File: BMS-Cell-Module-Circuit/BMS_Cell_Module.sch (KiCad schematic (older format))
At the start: 34 parts, among them J1 Conn_01x02_Female, J2 Conn_01x04_Female, J3 Conn_01x04_Female, J4 Conn Female, J5 Conn Male, M1 SI2312BDS-T1-E3, U1 MCP1703A-3302_SOT223, U2 ADUM1250ARZ, U3 ATTINY85-20SU

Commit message: Project file changes
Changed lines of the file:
@@
 Text GLabel 10400 5400 2    60   Input ~ 12
 GND2
-Text Notes 5750 4450 2    60   ~ 0
+Text Notes 5750 4250 2    60   ~ 0
 Input battery voltage resistor \ndivider 517K vs 680K\n4.5V maps to 2.55V
 Text Notes 1150 5350 0    60   ~ 0
@@
 P 1250 5550
 F 0 "D1" H 1250 5650 50  0000 C CNN
-F 1 "SE30AFG-M3/6A" V 1150 5900 50  0000 C CNN
+F 1 "SE30AFG-M3/6A" V 1250 6050 50  0000 C CNN
 F 2 "Diodes_SMD:D_SMA" H 1250 5550 50  0001 C CNN
 F 3 "http://uk.farnell.com/vishay/se30afg-m3-6a/rectifier-esd-400v-3a-do-221ac/dp/2313878" H 1250 5550 50  0001 C CNN
@@
 P 1650 5550
 F 0 "F1" V 1730 5550 50  0000 C CNN
-F 1 "MC36232 1.5A 24V" V 1850 6150 50  0000 C CNN
+F 1 "MC36232 1.5A 24V" V 1550 5650 50  0000 C CNN
 F 2 "Resistors_SMD:R_1812_HandSoldering" V 1580 5550 50  0001 C CNN
 F 3 "http://uk.farnell.com/multicomp/mc36232/fuse-ptc-reset-smd-24v-1-5a/dp/1861171" H 1650 5550 50  0001 C CNN
@@
 U 1 1 5A08E265
 P 5600 6650
-F 0 "J5" H 5600 6950 50  0000 C CNN
-F 1 "Conn Male" H 5700 6200 50  0000 C CNN
+F 0 "J5" H 5600 7150 50  0000 C CNN
+F 1 "Conn Male" V 5550 6650 50  0000 C CNN
 F 2 "Pin_Headers:Pin_Header_Angled_1x10_Pitch2.54mm" H 5600 6650 50  0001 C CNN
 F 3 "" H 5600 6650 50  0001 C CNN
@@
 U 1 1 5A08F09E
 P 5250 6650
-F 0 "J4" H 5250 6950 50  0000 C CNN
-F 1 "Conn Female" H 5200 7050 50  0000 C CNN
+F 0 "J4" H 5300 7150 50  0000 C CNN
+F 1 "Conn Female" V 5300 6650 50  0000 C CNN
 F 2 "Socket_Strips:Socket_Strip_Angled_1x10_Pitch2.54mm" H 5250 6650 50  0001 C CNN
 F 3 "" H 5250 6650 50  0001 C CNN
@@
 	1    0    0    -1
 $EndComp
-Text GLabel 5800 7400 2    60   Input ~ 0
+Text GLabel 5900 7150 2    60   Input ~ 0
 GND2
 Text GLabel 1400 5050 1    60   Input ~ 12
@@
 Connection ~ 3800 3400
 Wire Wire Line
-	6200 2550 6200 6750
-Wire Wire Line
-	6050 2550 6050 6950
+	6200 2550 6200 3100
+Wire Wire Line
+	6200 3100 6200 6750
+Wire Wire Line
+	6050 2550 6050 3500
+Wire Wire Line
+	6050 3500 6050 6950
 Connection ~ 6350 3500
 Connection ~ 6050 3500
@@
 Connection ~ 6200 3100
 Wire Wire Line
-	6350 2550 6350 3500
+	6350 2550 6350 3250
+Wire Wire Line
+	6350 3250 6350 3400
+Wire Wire Line
+	6350 3400 6350 3500
 Wire Wire Line
 	6350 3400 6350 3250
@@
 Connection ~ 9600 5400
 Wire Wire Line
-	9350 4900 9800 4900
+	9350 4900 9400 4900
+Wire Wire Line
+	9400 4900 9600 4900
+Wire Wire Line
+	9600 4900 9800 4900
 Connection ~ 9600 4900
 Wire Wire Line
@@
 Connection ~ 9700 5400
 Wire Wire Line
-	5450 5050 5450 5450
+	5450 5050 5450 5200
+Wire Wire Line
+	5450 5200 5450 5450
 Wire Wire Line
 	5450 5750 5450 5850
@@
 	4200 5150 4600 5150
 Wire Wire Line
-	4200 5150 4200 5450
+	4200 5150 4200 5400
+Wire Wire Line
+	4200 5400 4200 5450
 Wire Wire Line
 	4200 3400 4200 4850
@@
 Connection ~ 5450 5850
 Wire Wire Line
-	4200 5400 6650 5400
+	4200 5400 6450 5400
+Wire Wire Line
+	6450 5400 6650 5400
 Connection ~ 4200 5400
 Wire Wire Line
-	10300 4150 10300 4400
+	10300 4150 10300 4250
+Wire Wire Line
+	10300 4250 10300 4400
 Wire Wire Line
 	10300 3850 10300 3750
@@
 	10300 4700 10300 4750
 Wire Wire Line
-	9350 5400 10400 5400
+	9350 5400 9600 5400
+Wire Wire Line
+	9600 5400 9700 5400
+Wire Wire Line
+	9700 5400 10300 5400
+Wire Wire Line
+	10300 5400 10400 5400
 Connection ~ 10300 5400
 Wire Wire Line
@@
 	6150 4250 6150 5000
 Wire Wire Line
-	6100 5000 6650 5000
+	6100 5000 6150 5000
+Wire Wire Line
+	6150 5000 6650 5000
 Connection ~ 10300 4250
 Wire Wire Line
@@
 	5950 1300 5900 1400
 Wire Wire Line
-	5900 1400 5900 1850
-Wire Wire Line
-	6050 1300 6050 1850
-Wire Wire Line
-	6200 1400 6200 1850
+	5900 1400 5900 1550
+Wire Wire Line
+	5900 1550 5900 1850
+Wire Wire Line
+	6050 1300 6050 1600
+Wire Wire Line
+	6050 1600 6050 1850
+Wire Wire Line
+	6200 1400 6200 1650
+Wire Wire Line
+	6200 1650 6200 1850
 Wire Wire Line
 	6200 1400 6150 1300
@@
 	6250 1300 6350 1400
 Wire Wire Line
-	6350 1400 6350 1850
+	6350 1400 6350 1700
+Wire Wire Line
+	6350 1700 6350 1850
 Wire Wire Line
 	6350 1700 7050 1700
@@
 Connection ~ 5850 5850
 Wire Wire Line
-	1700 6100 1700 7250
-Wire Wire Line
-	1550 6850 2150 6850
-Wire Wire Line
-	3050 6850 3050 7250
+	1700 6100 1700 6850
+Wire Wire Line
+	1700 6850 1700 7250
+Wire Wire Line
+	1550 6850 1700 6850
+Wire Wire Line
+	1700 6850 2150 6850
+Wire Wire Line
+	3050 6850 3050 7100
+Wire Wire Line
+	3050 7100 3050 7250
 Connection ~ 1700 6850
 Wire Wire Line
@@
 	800  5550 800  5800
 Wire Wire Line
-	800  5550 1100 5550
+	800  5550 1050 5550
+Wire Wire Line
+	1050 5550 1100 5550
 Wire Wire Line
 	1400 5550 1500 5550
@@
 	3450 6950 4550 6950
 Wire Wire Line
-	4550 6550 4550 7000
-Wire Wire Line
-	3700 7450 5050 7450
-Wire Wire Line
-	5050 7150 5050 7550
+	4550 6550 4550 6950
+Wire Wire Line
+	4550 6950 4550 7000
+Wire Wire Line
+	3700 7450 4550 7450
+Wire Wire Line
+	4550 7450 5050 7450
+Wire Wire Line
+	5050 7150 5050 7450
+Wire Wire Line
+	5050 7450 5150 7450
 Wire Wire Line
 	6650 5300 6150 5300
@@
 	6150 6550 5800 6550
 Wire Wire Line
-	4200 5850 9700 5850
+	4200 5850 5450 5850
+Wire Wire Line
+	5450 5850 5700 5850
+Wire Wire Line
+	5700 5850 5850 5850
+Wire Wire Line
+	5850 5850 9700 5850
 Connection ~ 1950 5550
 Wire Wire Line
-	2750 3400 3050 3400
+	2750 3400 2900 3400
+Wire Wire Line
+	2900 3400 3050 3400
 Wire Wire Line
 	4050 3400 4050 3550
 Connection ~ 4050 3400
 Wire Wire Line
-	3650 3400 6450 3400
-Wire Wire Line
-	2600 3050 5900 3050
-Wire Wire Line
-	5150 5200 6650 5200
+	3650 3400 3800 3400
+Wire Wire Line
+	3800 3400 3900 3400
+Wire Wire Line
+	3900 3400 4050 3400
+Wire Wire Line
+	4050 3400 4200 3400
+Wire Wire Line
+	4200 3400 6350 3400
+Wire Wire Line
+	6350 3400 6450 3400
+Wire Wire Line
+	2600 3050 2900 3050
+Wire Wire Line
+	2900 3050 3350 3050
+Wire Wire Line
+	3350 3050 3800 3050
+Wire Wire Line
+	3800 3050 5600 3050
+Wire Wire Line
+	5600 3050 5900 3050
+Wire Wire Line
+	5150 5200 5450 5200
+Wire Wire Line
+	5450 5200 5700 5200
+Wire Wire Line
+	5700 5200 6650 5200
 Wire Wire Line
 	1150 5050 1150 4800
@@
 Wire Wire Line
 	1950 6100 1950 5550
-Text GLabel 5050 7550 2    60   Input ~ 0
+Text GLabel 5150 7450 2    60   Input ~ 0
 GND
 Connection ~ 5050 7450
@@
 Wire Wire Line
 	5050 6850 5050 6950
-Connection ~ 3050 6850
 Wire Wire Line
 	5450 4300 5950 4300
@@
 	2750 5950 5800 5950
 Wire Wire Line
-	5800 7150 5800 7400
+	5800 7150 5900 7150
 Wire Wire Line
 	5800 7050 6450 7050
@@
 	900  5150 1050 5250
 Wire Wire Line
-	1050 5250 1050 5800
+	1050 5250 1050 5550
+Wire Wire Line
+	1050 5550 1050 5800
 Wire Wire Line
 	5050 6450 4950 6450

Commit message: Started redesign of PCB
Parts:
- removed D3: LED RED, LEDs:LED_1206_HandSoldering, symbol LED
- removed J4: Conn Female, Socket_Strips:Socket_Strip_Angled_1x10_Pitch2.54mm, symbol Conn_01x10_Female
- removed J5: Conn Male, Pin_Headers:Pin_Header_Angled_1x10_Pitch2.54mm, symbol Conn_01x10_Male
- removed R11: 510R, Resistors_SMD:R_1206_HandSoldering, symbol R
- removed R13: 2K2, Resistors_SMD:R_1206_HandSoldering, symbol R
- added ISP1: Conn_02x03_Odd_Even, Pin_Headers:Pin_Header_Straight_2x03_Pitch2.54mm, symbol Conn_02x03_Odd_Even
- C1, C2: value 1uF -> 1uF Ceramic; footprint Capacitors_SMD:C_1210_HandSoldering -> Capacitors_SMD:C_1206_HandSoldering
- C3, C4, C5: footprint Capacitors_SMD:C_1210_HandSoldering -> Capacitors_SMD:C_1206_HandSoldering
- J2, J3: footprint Connectors_JST:JST_PH_S4B-PH-SM4-TB_04x2.00mm_Angled -> Connectors_JST:JST_PH_S4B-PH-K_04x2.00mm_Angled
- R12: value 510R -> 2K2
- R2: value 47R 1/4W -> 47R
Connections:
- net BATT+ is gone; now on an unnamed net: D2.2 (A), F1.1, R1.2
- net GND2 is gone; now on net GND: C1.1, C2.1, C3.2, C4.2, C5.2, R12.2, R4.2, R7.2, U1.2 (GND), U2.5 (GND2), U3.4 (GND)
- net VCC is gone; now on net +BATT: D1.2 (A), J1.1 (Pin_1)
- net +3V3: now also ISP1.2 (Pin_2)
- net GND: now also ISP1.6 (Pin_6)
- net at R3.2, R4.1, TH1.2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: now also ISP1.5 (Pin_5)
- net at U3.3 (PB4(XTAL2/CLKO/OC1B/ADC2/PCINT4)): now also M1.1 (GATE), R9.1
- net at U3.5 (PB0(MOSI/DI/SDA/AIN0/OC0A/~OC1A~/AREF/PCINT0)): now also R10.1, U2.7 (SDA2), ISP1.4 (Pin_4)
- net at D4.2 (A), U3.6 (PB1(MISO/DO/AIN1/OC0B/OC1A/PCINT1)): now also ISP1.1 (Pin_1)
- net at U3.7 (PB2(SCK/USCK/SCL/T0/INT0/ADC1/PCINT2)): now also R8.2, U2.6 (SCL2), ISP1.3 (Pin_3)
- net +BATT: now reaches R5.1
- no-connect marks 2 -> 0
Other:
- moved on the sheet: R12

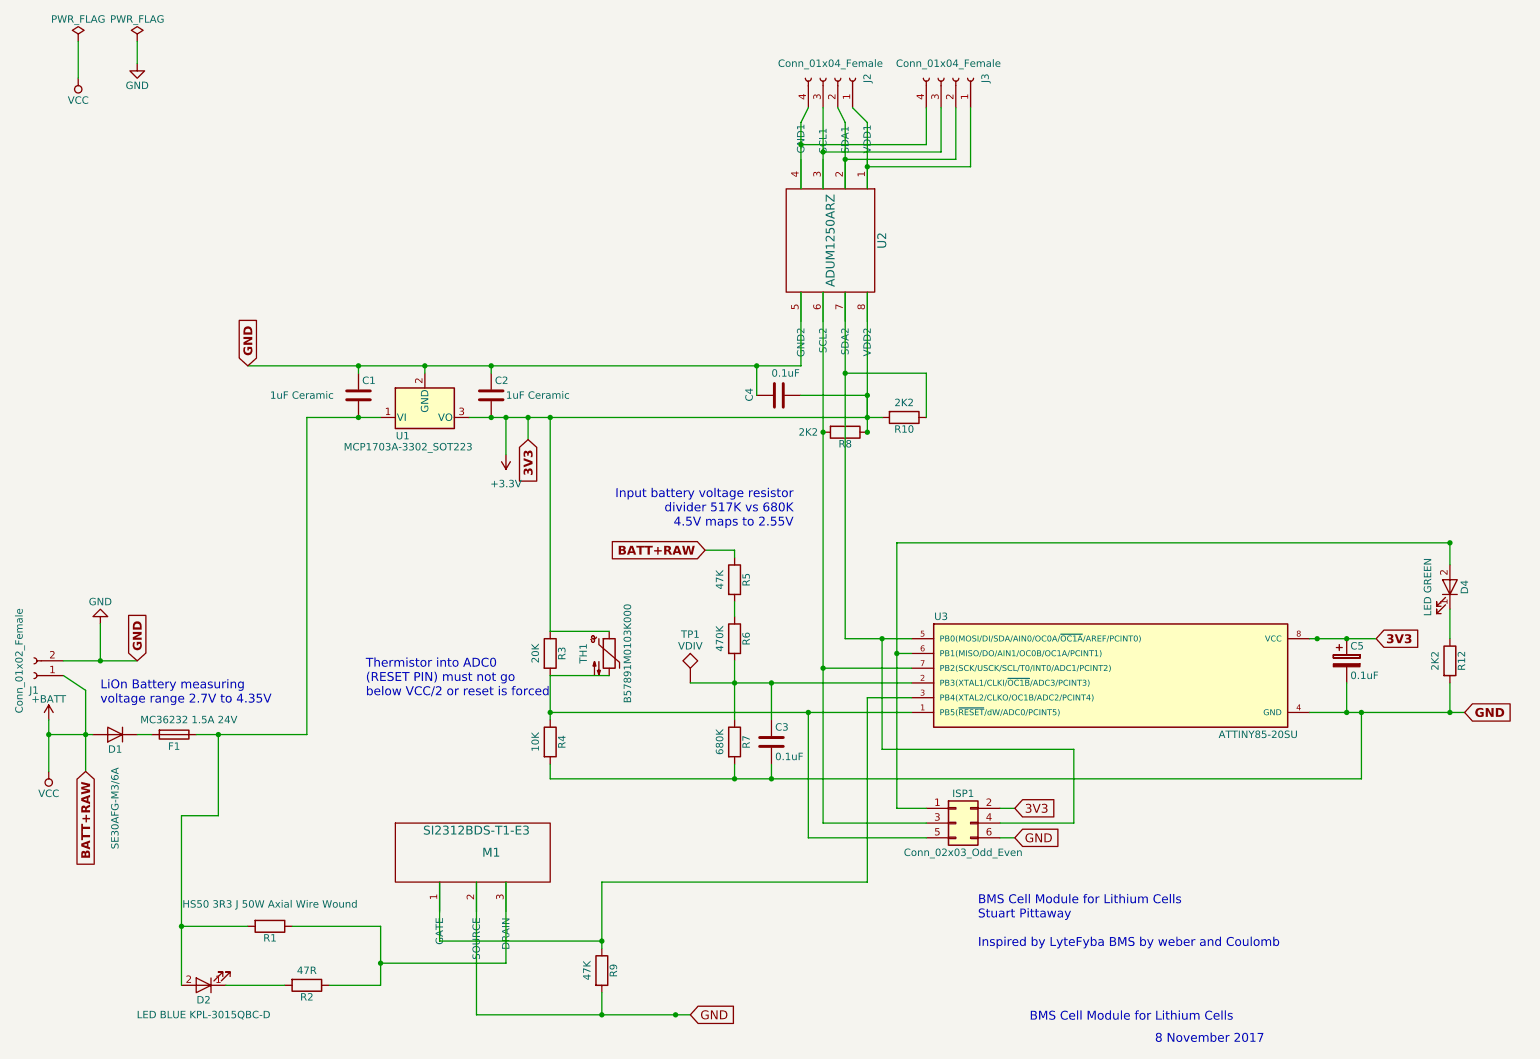
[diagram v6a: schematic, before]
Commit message: Custom PCB footprints
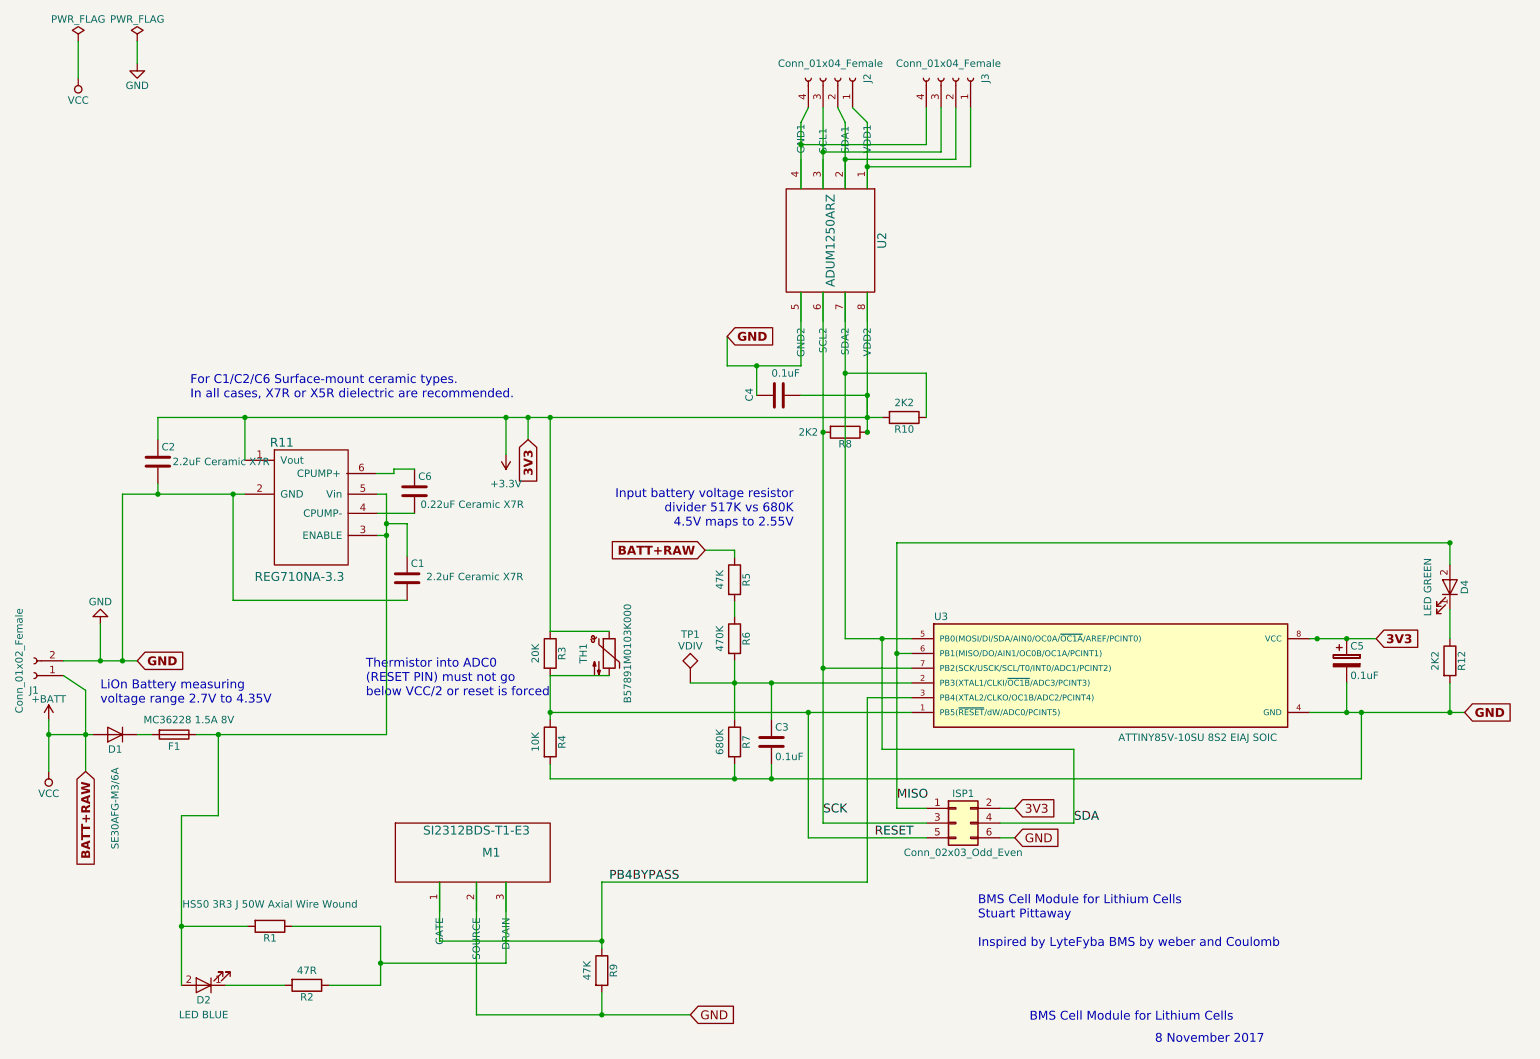
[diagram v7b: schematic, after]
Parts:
- removed U1: MCP1703A-3302_SOT223, TO_SOT_Packages_SMD:SOT-223-3_TabPin2, symbol MCP1703A-3302_SOT223
- added C6: 0.22uF Ceramic X7R, Capacitors_SMD:C_1206_HandSoldering, symbol C
- added R11: REG710NA-3.3, TO_SOT_Packages_SMD:SOT-23-6_Handsoldering, symbol REG710
- C1, C2: value 1uF Ceramic -> 2.2uF Ceramic X7R
- D1: footprint Diodes_SMD:D_SMA -> ATTINY:DO-221AC
- D2: value LED BLUE KPL-3015QBC-D -> LED BLUE
- F1: value MC36232 1.5A 24V -> MC36228 1.5A 8V
- J1: footprint Connectors_JST:JST_SFH_SM02B-SFHRS-TF_02x1.80mm_Angled -> Connectors_JST:JST_PH_S2B-PH-K_02x2.00mm_Angled
- U2: footprint SMD_Packages:SOIC-8-N -> adum1250:ADUM1250
- U3: value ATTINY85-20SU -> ATTINY85V-10SU 8S2 EIAJ SOIC; footprint Housings_SOIC:SOIC-8_3.9x4.9mm_Pitch1.27mm -> ATTINY:ATTINY85V
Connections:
- net +3V3: now also C2.1, R11.1 (Vout); no longer C2.2
- net GND: now also C1.2, C2.2, R11.2 (GND); no longer C1.1, C2.1
- net RESET: now reaches ISP1.5 (Pin_5), R3.2, R4.1, TH1.2, U3.1 (PB5(~RESET~/dW/ADC0/PCINT5))
- net PB4BYPASS: now reaches M1.1 (GATE), R9.1, U3.3 (PB4(XTAL2/CLKO/OC1B/ADC2/PCINT4))
- net SDA: now reaches ISP1.4 (Pin_4), R10.1, U2.7 (SDA2), U3.5 (PB0(MOSI/DI/SDA/AIN0/OC0A/~OC1A~/AREF/PCINT0))
- net MISO: now reaches D4.2 (A), ISP1.1 (Pin_1), U3.6 (PB1(MISO/DO/AIN1/OC0B/OC1A/PCINT1))
- net SCK: now reaches ISP1.3 (Pin_3), R8.2, U2.6 (SCL2), U3.7 (PB2(SCK/USCK/SCL/T0/INT0/ADC1/PCINT2))
- net at D2.2 (A), F1.1, R1.2: now also C1.1, R11.3 (ENABLE), R11.5 (Vin); no longer C1.2
- new net: C6.2, R11.4 (CPUMP-)
- new net: C6.1, R11.6 (CPUMP+)
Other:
- note added: "For C1/C2/C6 Surface-mount ceramic types. \nIn all cases, X7R or X5R dielectric are recommended."
- moved on the sheet: C1, C2

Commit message: Updated PCB layout
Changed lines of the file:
@@
 Connection ~ 6200 3100
 Wire Wire Line
-	6350 2550 6350 3250
-Wire Wire Line
-	6350 3250 6350 3400
-Wire Wire Line
-	6350 3400 6350 3500
+	6350 2550 6350 3500
 Wire Wire Line
 	6350 3400 6350 3250
@@
 Connection ~ 9600 5400
 Wire Wire Line
-	9350 4900 9400 4900
-Wire Wire Line
-	9400 4900 9600 4900
-Wire Wire Line
-	9600 4900 9800 4900
+	9350 4900 9800 4900
 Connection ~ 9600 4900
 Wire Wire Line
@@
 Connection ~ 9700 5400
 Wire Wire Line
-	5450 5050 5450 5200
-Wire Wire Line
-	5450 5200 5450 5450
+	5450 5050 5450 5450
 Wire Wire Line
 	5450 5750 5450 5850
@@
 	4200 5150 4600 5150
 Wire Wire Line
-	4200 5150 4200 5400
-Wire Wire Line
-	4200 5400 4200 5450
+	4200 5150 4200 5450
 Wire Wire Line
 	4200 3400 4200 4850
@@
 Connection ~ 5450 5850
 Wire Wire Line
-	4200 5400 5950 5400
-Wire Wire Line
-	5950 5400 6650 5400
+	4200 5400 6650 5400
 Connection ~ 4200 5400
 Wire Wire Line
@@
 	10300 4700 10300 4900
 Wire Wire Line
-	9350 5400 9600 5400
-Wire Wire Line
-	9600 5400 9700 5400
-Wire Wire Line
-	9700 5400 10300 5400
-Wire Wire Line
-	10300 5400 10400 5400
+	9350 5400 10400 5400
 Connection ~ 10300 5400
 Connection ~ 9400 4900
@@
 	6550 4250 10300 4250
 Wire Wire Line
-	6550 4250 6550 5000
-Wire Wire Line
-	6550 5000 6550 6050
+	6550 4250 6550 6050
 Wire Wire Line
 	6550 5000 6650 5000
@@
 	5950 1300 5900 1400
 Wire Wire Line
-	5900 1400 5900 1550
-Wire Wire Line
-	5900 1550 5900 1850
-Wire Wire Line
-	6050 1300 6050 1600
-Wire Wire Line
-	6050 1600 6050 1850
-Wire Wire Line
-	6200 1400 6200 1650
-Wire Wire Line
-	6200 1650 6200 1850
+	5900 1400 5900 1850
+Wire Wire Line
+	6050 1300 6050 1850
+Wire Wire Line
+	6200 1400 6200 1850
 Wire Wire Line
 	6200 1400 6150 1300
@@
 	6250 1300 6350 1400
 Wire Wire Line
-	6350 1400 6350 1700
-Wire Wire Line
-	6350 1700 6350 1850
+	6350 1400 6350 1850
 Wire Wire Line
 	6350 1700 7050 1700
@@
 Connection ~ 5900 1550
 Wire Wire Line
-	900  5050 1150 5050
-Wire Wire Line
-	1150 5050 1300 5050
-Wire Wire Line
-	1300 5050 1400 5050
+	900  5050 1400 5050
 Connection ~ 1050 5550
 Connection ~ 1150 5050
@@
 	3450 6950 3450 6550
 Wire Wire Line
-	1700 6100 1700 6850
-Wire Wire Line
-	1700 6850 1700 7250
-Wire Wire Line
-	3050 6850 3050 7100
-Wire Wire Line
-	3050 7100 3050 7250
+	1700 6100 1700 7250
+Wire Wire Line
+	3050 6850 3050 7250
 Connection ~ 1700 6850
 Wire Wire Line
@@
 Connection ~ 3050 7100
 Wire Wire Line
-	800  5550 1050 5550
-Wire Wire Line
-	1050 5550 1100 5550
+	800  5550 1100 5550
 Wire Wire Line
 	1400 5550 1500 5550
@@
 	3450 6950 4550 6950
 Wire Wire Line
-	4550 6550 4550 6950
-Wire Wire Line
-	4550 6950 4550 7000
-Wire Wire Line
-	3700 7450 4550 7450
-Wire Wire Line
-	4550 7450 5150 7450
+	4550 6550 4550 7000
+Wire Wire Line
+	3700 7450 5150 7450
 Wire Wire Line
 	6650 5300 6350 5300
@@
 	6350 6550 4550 6550
 Wire Wire Line
-	4200 5850 5450 5850
-Wire Wire Line
-	5450 5850 5700 5850
-Wire Wire Line
-	5700 5850 9700 5850
+	4200 5850 9700 5850
 Wire Wire Line
 	4050 3400 4050 3550
 Connection ~ 4050 3400
 Wire Wire Line
-	1540 3400 2130 3400
-Wire Wire Line
-	2130 3400 3900 3400
-Wire Wire Line
-	3900 3400 4050 3400
-Wire Wire Line
-	4050 3400 4200 3400
-Wire Wire Line
-	4200 3400 6350 3400
-Wire Wire Line
-	6350 3400 6450 3400
-Wire Wire Line
-	5150 5200 5450 5200
-Wire Wire Line
-	5450 5200 5700 5200
-Wire Wire Line
-	5700 5200 6650 5200
+	1540 3400 6450 3400
+Wire Wire Line
+	5150 5200 6650 5200
 Wire Wire Line
 	1150 5050 1150 4800
@@
 Connection ~ 4550 6950
 Wire Wire Line
-	6200 4900 6450 4900
-Wire Wire Line
-	6450 4900 6650 4900
+	6200 4900 6650 4900
 Wire Wire Line
 	6050 5100 6650 5100
@@
 	900  5150 1050 5250
 Wire Wire Line
-	1050 5250 1050 5550
-Wire Wire Line
-	1050 5550 1050 5800
+	1050 5250 1050 5800
 $Comp
 L Conn_02x03_Odd_Even ISP1
@@
 Connection ~ 6050 5100
 Wire Wire Line
-	6050 2550 6050 3500
-Wire Wire Line
-	6050 3500 6050 5100
-Wire Wire Line
-	6050 5100 6050 6150
+	6050 2550 6050 6150
 Wire Wire Line
 	6050 6150 6750 6150
 Wire Wire Line
-	6200 2550 6200 3100
-Wire Wire Line
-	6200 3100 6200 4900
+	6200 2550 6200 4900
 Wire Wire Line
 	6450 4900 6450 5650
@@
 Connection ~ 800  5550
 Wire Wire Line
-	800  5450 800  5550
-Wire Wire Line
-	800  5550 800  5800
+	800  5450 800  5800
 Connection ~ 1300 5050
 Text Label 7750 6150 0    60   ~ 0
@@
 PB4BYPASS
 Wire Wire Line
-	5400 3050 5600 3050
-Wire Wire Line
-	5600 3050 5900 3050
+	5400 3050 5900 3050
 Text GLabel 5400 2850 2    60   Input ~ 12
 GND
@@
 	3030 3920 3090 3920
 Wire Wire Line
-	3090 3920 3090 4120
-Wire Wire Line
-	3090 4120 3090 4200
-Wire Wire Line
-	3090 4200 3090 5550
+	3090 3920 3090 5550
 Wire Wire Line
 	2130 3690 2130 3400
 Wire Wire Line
-	3090 5550 1950 5550
-Wire Wire Line
-	1950 5550 1800 5550
+	3090 5550 1800 5550
 Wire Wire Line
 	1950 6100 1950 5550
@@
 	1300 5050 1300 3920
 Wire Wire Line
-	1300 3920 1540 3920
-Wire Wire Line
-	1540 3920 2050 3920
-Wire Wire Line
-	2050 3920 2130 3920
+	1300 3920 2130 3920
 $Comp
 L C C6
